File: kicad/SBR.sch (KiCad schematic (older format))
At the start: 29 parts

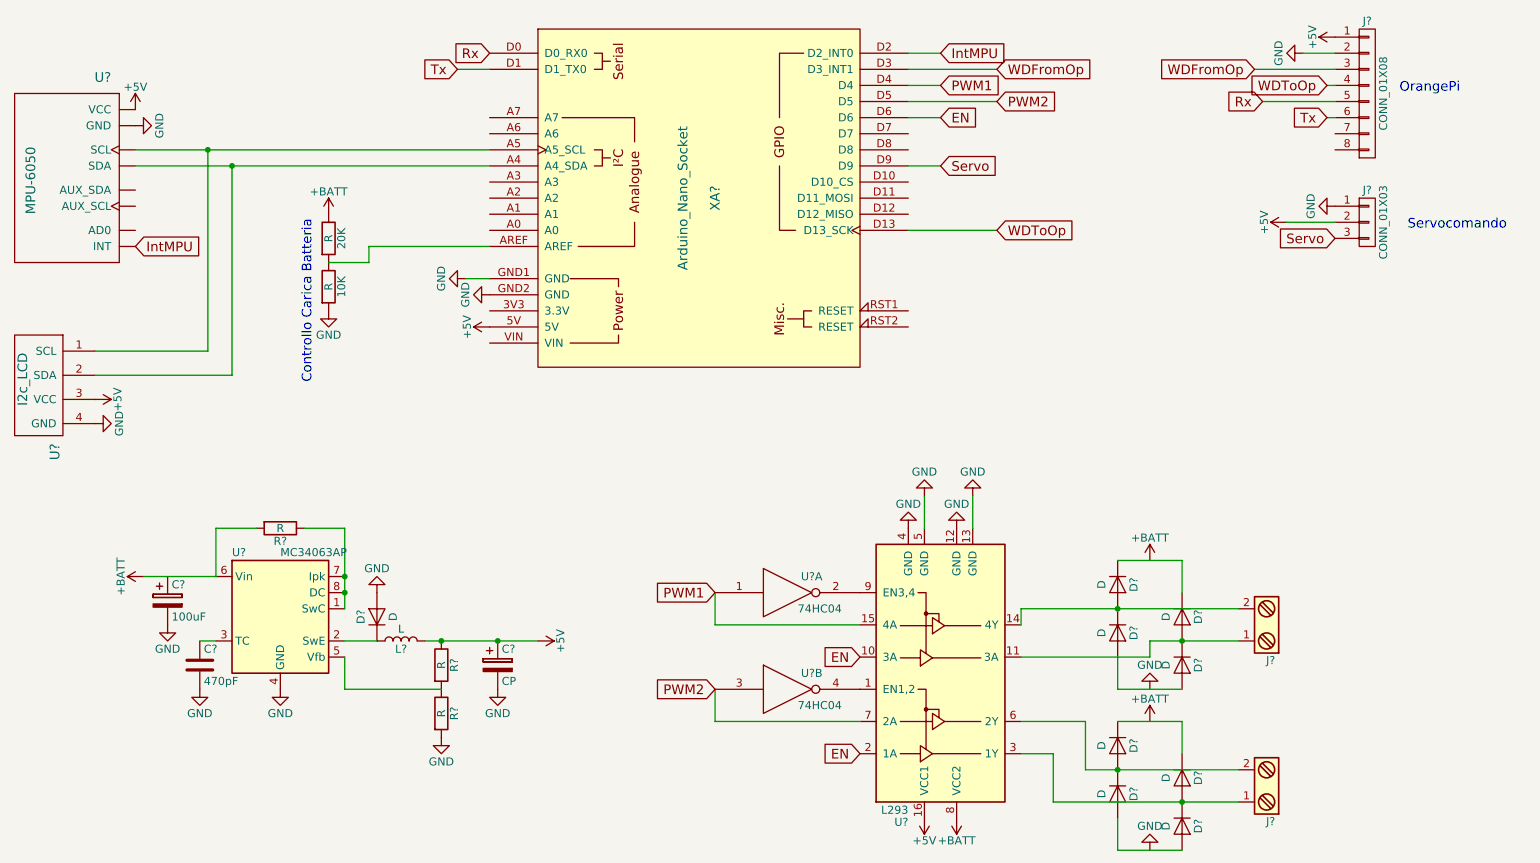
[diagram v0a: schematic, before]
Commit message: Sch update and 3D model for motor bracket
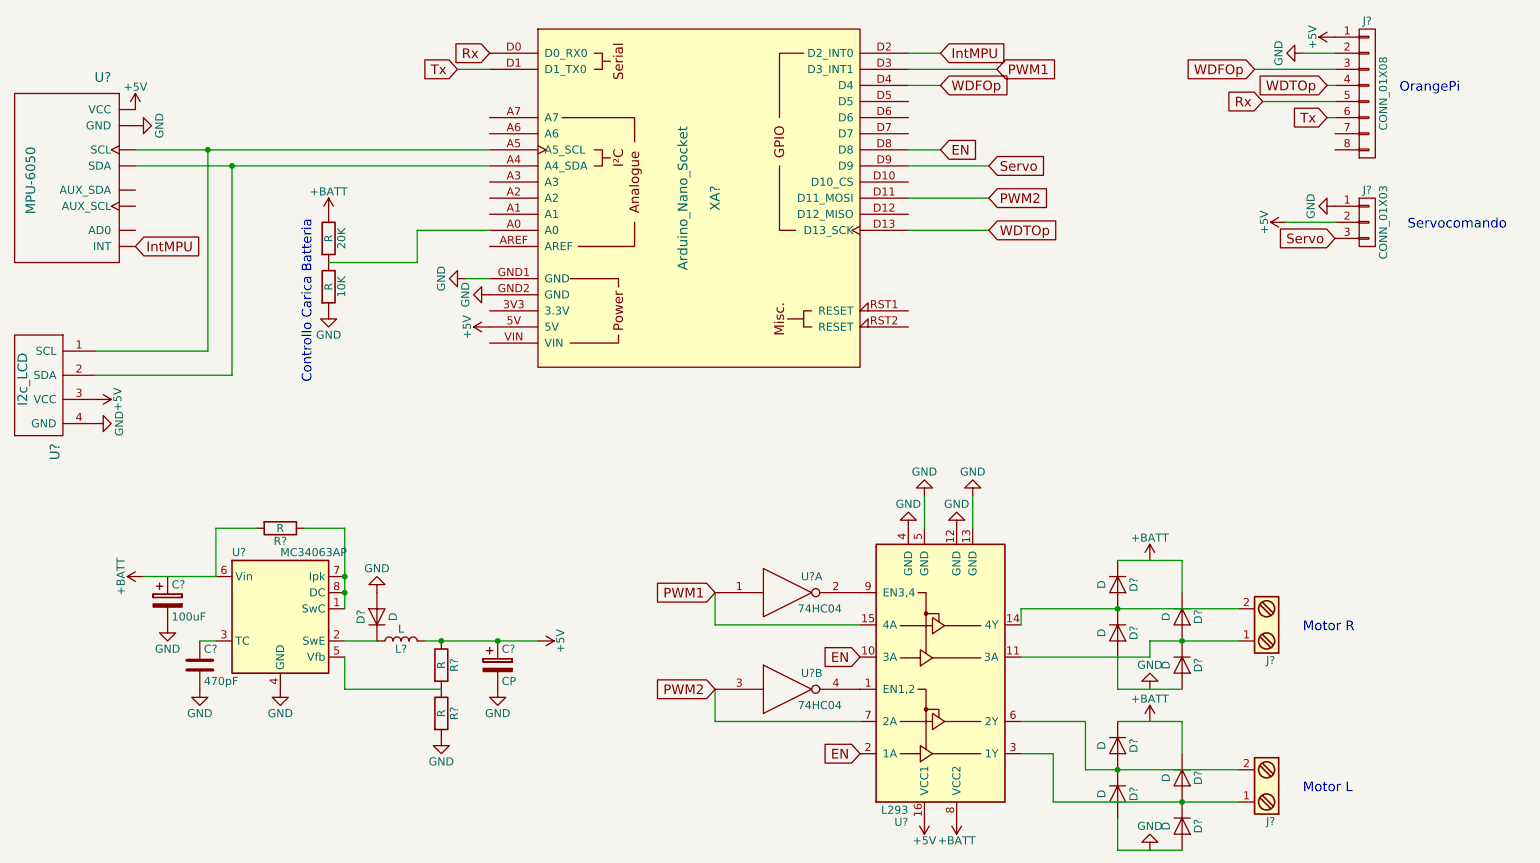
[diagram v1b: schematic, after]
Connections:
- net EN: now also XA?.D8; no longer XA?.D6
- net PWM1: now also XA?.D3 (D3_INT1); no longer XA?.D4
- net PWM2: now also XA?.D11 (D11_MOSI); no longer XA?.D5
- net at XA?.A0: now also 10K.1, 20K.2
- net WDFromOp renamed WDFOp
- net WDFOp: now also XA?.D4; no longer XA?.D3 (D3_INT1)
- net WDToOp renamed WDTOp
- now unconnected: XA?.AREF
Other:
- note added: "Motor L\n"
- note added: "Motor R"
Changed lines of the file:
@@
 Wire Wire Line
 	1900 2050 4100 2050
-Text GLabel 6900 1550 2    60   Input ~ 0
+Text GLabel 7250 1450 2    60   Input ~ 0
 PWM1
-Text GLabel 7250 1650 2    60   Input ~ 0
+Text GLabel 7200 2250 2    60   Input ~ 0
 PWM2
-Wire Wire Line
-	7250 1650 6700 1650
 Wire Wire Line
 	6900 1550 6700 1550
@@
 Text GLabel 6400 5700 0    60   Input ~ 0
 EN
-Text GLabel 6900 1750 2    60   Input ~ 0
+Text GLabel 6900 1950 2    60   Input ~ 0
 EN
-Wire Wire Line
-	6900 1750 6700 1750
 Text GLabel 1900 2550 2    60   Input ~ 0
 IntMPU
@@
 	0    -1   -1   0
 $EndComp
-Text GLabel 7250 1450 2    60   Input ~ 0
-WDFromOp
+Text GLabel 6900 1550 2    60   Input ~ 0
+WDFOp
 Wire Wire Line
 	6700 1350 6900 1350
 Wire Wire Line
 	7250 1450 6700 1450
-Text GLabel 7250 2450 2    60   Input ~ 0
-WDToOp
-Wire Wire Line
-	7250 2450 6700 2450
+Text GLabel 7200 2450 2    60   Input ~ 0
+WDTOp
 $Comp
 L +5V #PWR?
@@
 $EndComp
 Text GLabel 8850 1450 0    60   Input ~ 0
-WDFromOp
+WDFOp
 Text GLabel 9300 1550 0    60   Input ~ 0
-WDToOp
+WDTOp
 Wire Wire Line
 	9150 1350 9350 1350
@@
 Wire Wire Line
 	9300 1550 9350 1550
-Text GLabel 6900 2050 2    60   Input ~ 0
+Text GLabel 7200 2050 2    60   Input ~ 0
 Servo
-Wire Wire Line
-	6700 2050 6900 2050
 Text GLabel 9350 2500 0    60   Input ~ 0
 Servo
@@
 	1    0    0    -1
 $EndComp
-Wire Wire Line
-	4100 2550 3350 2550
-Wire Wire Line
-	3350 2550 3350 2650
-Wire Wire Line
-	3350 2650 3100 2650
 $Comp
 L +BATT #PWR?
@@
 Text Notes 3000 3400 1    60   ~ 0
 Controllo Carica Batteria
+Wire Wire Line
+	3100 2650 3650 2650
+Wire Wire Line
+	3650 2650 3650 2450
+Wire Wire Line
+	3650 2450 4100 2450
+Wire Wire Line
+	6900 1950 6700 1950
+Wire Wire Line
+	7200 2050 6700 2050
+Wire Wire Line
+	7200 2250 6700 2250
+Text Notes 9150 4950 0    60   ~ 0
+Motor R
+Text Notes 9150 5950 0    60   ~ 0
+Motor L\n
+Wire Wire Line
+	7200 2450 6700 2450
 $EndSCHEMATC

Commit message: Schematical update
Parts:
- D2, D3, D4, D5, D6, D7, D8, D9: renamed from D?; value D -> MUR120; footprint (none) -> Diodes_ThroughHole:Diode_DO-41_SOD81_Horizontal_RM10
- gave numbers to parts that had none: 18
- renumbered 10K to 10K1, 20K to 20K1
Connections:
- net EN: now also U5.1 (EN1,2), U5.9 (EN3,4); no longer U5.10 (3A), U5.2 (1A)
- net PWM1: now also U5.10 (3A); no longer U5.15 (4A)
- net PWM2: no longer U5.7 (2A)
- net at U4.4: no longer U5.1 (EN1,2)
- net at U4.2: now also U5.15 (4A); no longer U5.9 (EN3,4)
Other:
- moved on the sheet: U4A, U4B
